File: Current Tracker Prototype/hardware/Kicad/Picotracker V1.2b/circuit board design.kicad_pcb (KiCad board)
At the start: 2 copper layers, 47.4 x 20.1 mm, 54 parts, among them IC7 SPV1040, J1 Conn_01x10, J2 GND, J3 +SOL, J4 BATT_V+, J5 BATT_GND, J6 ICSS LOGO, J7 Conn_01x01, J8 Conn_01x01, Q1 Q_PMOS_GSD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

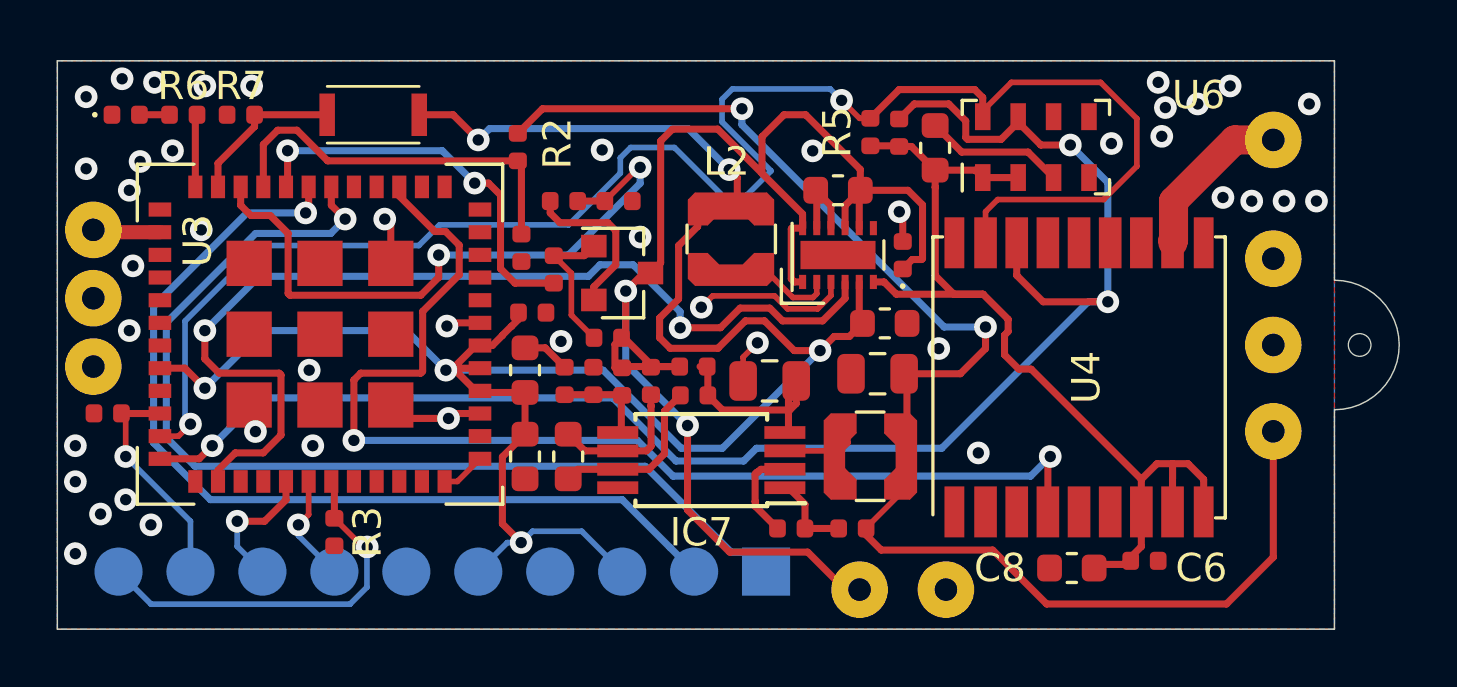
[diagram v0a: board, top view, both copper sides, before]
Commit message: connected pin 1 to pin 8 on spv1040 on the PCB
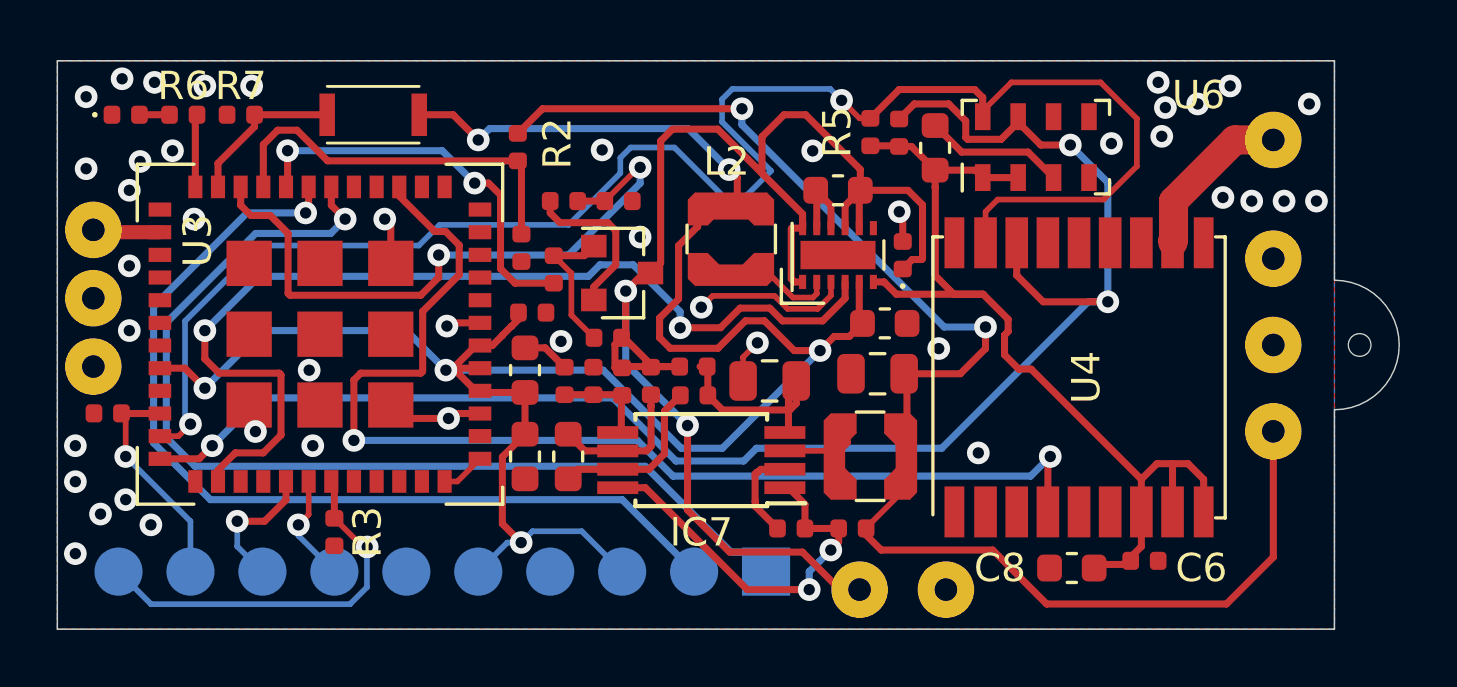
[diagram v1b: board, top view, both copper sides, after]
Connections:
- IC7 pad 8: (no net) -> Net-(C4-Pad1)
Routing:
- net Net-(C4-Pad1): track 2.87 -> 13.7 mm, vias 0 -> 2
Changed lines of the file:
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@@
     (thickness 0.6)
     (drawings 28)
-    (tracks 525)
+    (tracks 537)
     (zones 0)
     (modules 54)
@@
     (fp_line (start 2.2 -1.5) (end 2.2 1.5) (layer F.Fab) (width 0.15))
     (fp_line (start -1.2 -1.5) (end 2.2 -1.5) (layer F.Fab) (width 0.15))
-    (pad 8 smd rect (at 2.95 -0.975 180) (size 1.45 0.45) (layers F.Cu F.Paste F.Mask))
+    (pad 8 smd rect (at 2.95 -0.975 180) (size 1.45 0.45) (layers F.Cu F.Paste F.Mask)
+      (net 12 "Net-(C4-Pad1)"))
     (pad 7 smd rect (at 2.95 -0.325 180) (size 1.45 0.45) (layers F.Cu F.Paste F.Mask)
       (net 15 "Net-(C15-Pad1)"))
@@
   (via (at 269.24 164.592) (size 0.8) (drill 0.4) (layers F.Cu B.Cu) (net 1))
   (via (at 269.24 169.545) (size 0.8) (drill 0.4) (layers F.Cu B.Cu) (net 1))
-  (via (at 269.367 167.259) (size 0.8) (drill 0.4) (layers F.Cu B.Cu) (net 1))
+  (via (at 269.24 167.259) (size 0.8) (drill 0.4) (layers F.Cu B.Cu) (net 1))
   (via (at 267.335 173.609) (size 0.8) (drill 0.4) (layers F.Cu B.Cu) (net 1))
-  (via (at 271.78 165.989) (size 0.8) (drill 0.4) (layers F.Cu B.Cu) (net 1))
   (via (at 270.764 163.195) (size 0.8) (drill 0.4) (layers F.Cu B.Cu) (net 1))
   (via (at 268.224 176.022) (size 0.8) (drill 0.4) (layers F.Cu B.Cu) (net 1))
@@
   (via (at 305.816 161.671) (size 0.8) (drill 0.4) (layers F.Cu B.Cu) (net 1))
   (via (at 307.848 164.846) (size 0.8) (drill 0.4) (layers F.Cu B.Cu) (net 1))
+  (via (at 271.526 165.608) (size 0.8) (drill 0.4) (layers F.Cu B.Cu) (net 1))
   (segment (start 300.619 162.193) (end 300.619 161.993) (width 0.25) (layer F.Cu) (net 2) (status 30))
   (segment (start 300.018999 162.793001) (end 300.619 162.193) (width 0.25) (layer F.Cu) (net 2) (status 20))
@@
   (segment (start 292.608999 165.953001) (end 292.634 165.928) (width 0.25) (layer F.Cu) (net 11))
   (segment (start 293.009 167.828) (end 292.717227 167.828) (width 0.25) (layer F.Cu) (net 11) (status 10))
-  (segment (start 288.947212 175.879237) (end 288.947212 172.895136) (width 0.25) (layer F.Cu) (net 11))
-  (segment (start 290.432484 177.364509) (end 288.947212 175.879237) (width 0.25) (layer F.Cu) (net 11))
   (via (at 288.947212 172.895136) (size 0.8) (drill 0.4) (layers F.Cu B.Cu) (net 11))
-  (segment (start 294.513 178.689) (end 293.188509 177.364509) (width 0.25) (layer F.Cu) (net 11) (status 10))
   (segment (start 286.766 170.713924) (end 288.947212 172.895136) (width 0.25) (layer B.Cu) (net 11))
   (segment (start 286.766 168.147996) (end 286.766 170.713924) (width 0.25) (layer B.Cu) (net 11))
-  (segment (start 293.188509 177.364509) (end 290.432484 177.364509) (width 0.25) (layer F.Cu) (net 11))
   (segment (start 290.014 162.433) (end 291.574999 163.993999) (width 0.25) (layer F.Cu) (net 11))
   (segment (start 287.400996 167.513) (end 287.639 167.513) (width 0.25) (layer F.Cu) (net 11) (status 30))
@@
   (segment (start 288.417 162.433) (end 290.014 162.433) (width 0.25) (layer F.Cu) (net 11))
   (segment (start 287.999002 167.152998) (end 287.999002 162.850998) (width 0.25) (layer F.Cu) (net 11) (status 10))
+  (segment (start 288.947212 173.460821) (end 288.947212 172.895136) (width 0.25) (layer F.Cu) (net 11))
+  (segment (start 288.947212 175.879237) (end 288.947212 173.460821) (width 0.25) (layer F.Cu) (net 11))
+  (segment (start 293.004503 177.364509) (end 290.432484 177.364509) (width 0.25) (layer F.Cu) (net 11))
+  (segment (start 294.513 178.689) (end 294.328994 178.689) (width 0.25) (layer F.Cu) (net 11))
+  (segment (start 290.432484 177.364509) (end 288.947212 175.879237) (width 0.25) (layer F.Cu) (net 11))
+  (segment (start 294.328994 178.689) (end 293.004503 177.364509) (width 0.25) (layer F.Cu) (net 11))
   (segment (start 293.093 175.675) (end 293.093 176.53) (width 0.25) (layer F.Cu) (net 12) (status 20))
   (segment (start 292.51 175.092) (end 293.093 175.675) (width 0.25) (layer F.Cu) (net 12) (status 10))
   (segment (start 294.282 176.53) (end 293.093 176.53) (width 0.25) (layer F.Cu) (net 12) (status 30))
+  (via (at 293.243 178.689) (size 0.8) (drill 0.4) (layers F.Cu B.Cu) (net 12))
+  (segment (start 291.055 178.689) (end 293.243 178.689) (width 0.25) (layer F.Cu) (net 12))
+  (segment (start 286.483 175.092) (end 287.458 175.092) (width 0.25) (layer F.Cu) (net 12))
+  (segment (start 287.458 175.092) (end 291.055 178.689) (width 0.25) (layer F.Cu) (net 12))
+  (via (at 294.004994 177.292) (size 0.8) (drill 0.4) (layers F.Cu B.Cu) (net 12))
+  (segment (start 293.243 178.689) (end 293.243 178.053994) (width 0.25) (layer B.Cu) (net 12))
+  (segment (start 293.243 178.053994) (end 293.604995 177.691999) (width 0.25) (layer B.Cu) (net 12))
+  (segment (start 293.604995 177.691999) (end 294.004994 177.292) (width 0.25) (layer B.Cu) (net 12))
+  (segment (start 294.282 177.014994) (end 294.004994 177.292) (width 0.25) (layer F.Cu) (net 12))
+  (segment (start 294.282 176.53) (end 294.282 177.014994) (width 0.25) (layer F.Cu) (net 12))
   (segment (start 295.009 169.076) (end 295.009 167.828) (width 0.25) (layer F.Cu) (net 13) (status 30))
   (segment (start 295.224 169.291) (end 295.009 169.076) (width 0.25) (layer F.Cu) (net 13) (status 30))

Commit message: fully routed board
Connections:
- Q1 pad 2: Net-(Q1-Pad2) -> +BATT
- Q1 pad 3: +BATT -> Net-(Q1-Pad3)
- R15 pad 1: Net-(Q1-Pad2) -> Net-(Q1-Pad3)
- U3 pad 16: (no net) -> /GPS_EXTINT
- U4 pad 5: (no net) -> /GPS_EXTINT
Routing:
- net /GPS_EXTINT: track 0.00 -> 47.6 mm, vias 0 -> 2
- net Net-(Q1-Pad3): track 0.00 -> 9.43 mm
- net Net-(Q1-Pad2): track 5.84 -> 0.00 mm
- net /I2C1_SCL: track 59.5 -> 55.3 mm
- net +SOL: track 53.5 -> 56.7 mm
- net /BATT_VOLTS: track 22.6 -> 24.5 mm
- net GND: track 28.7 -> 29.9 mm, vias 44 -> 43
- net +BATT: track 53.0 -> 51.8 mm, vias 2 -> 3
- net /GPS_TIMEPULSE: track 40.2 -> 41.2 mm
- net /SENSOR_EN: track 35.4 -> 34.8 mm
